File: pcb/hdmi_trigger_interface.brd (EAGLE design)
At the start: 78.7 x 63.5 mm, 58 parts, among them U1 TPD12S016PWR, U2 TPD12S016PWR, Y1 SI514

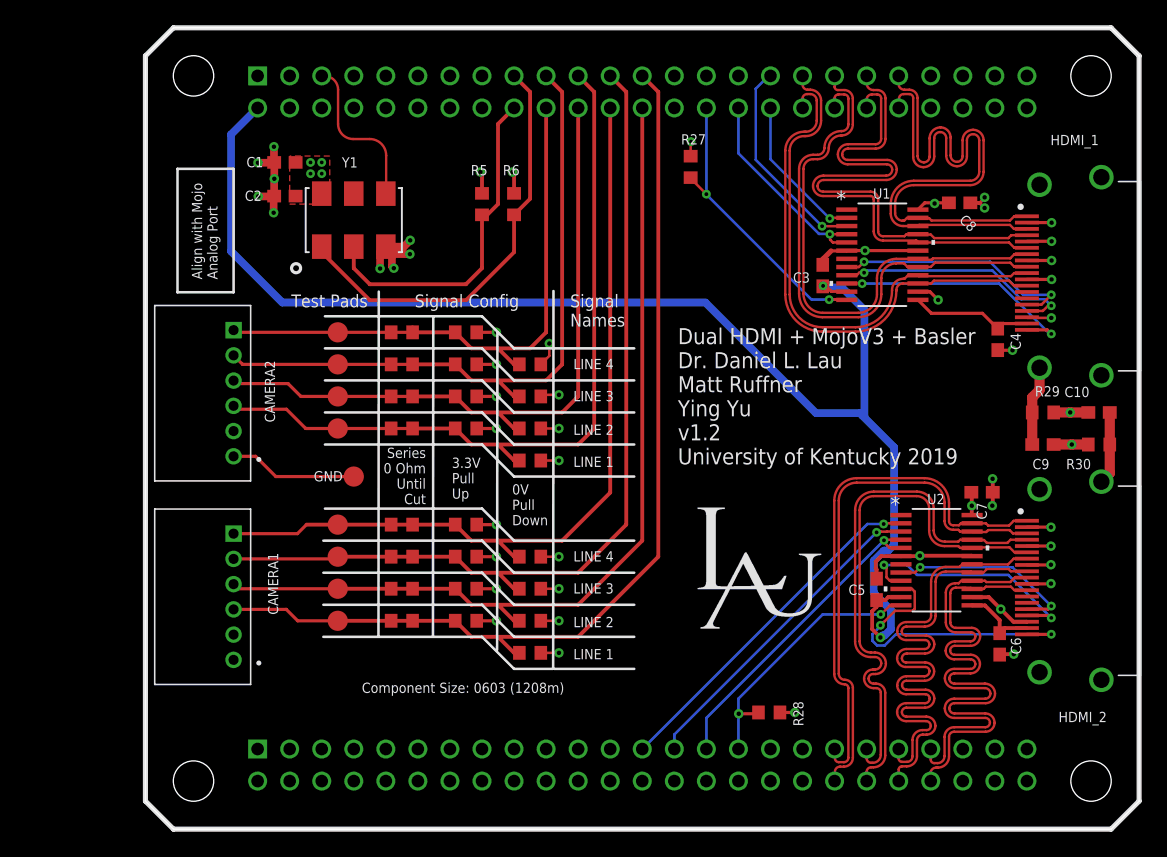
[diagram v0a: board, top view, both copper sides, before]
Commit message: ripped up old diff pairs, ready to route new 8/8 lines
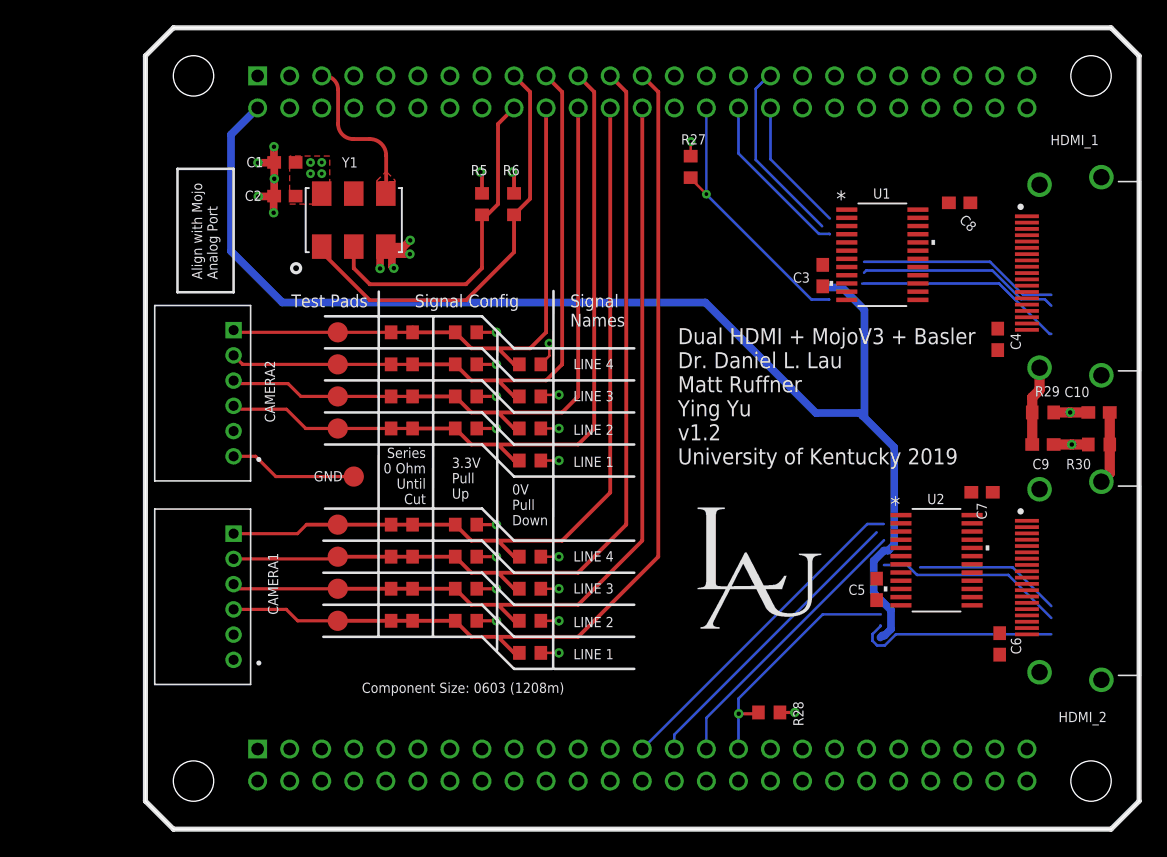
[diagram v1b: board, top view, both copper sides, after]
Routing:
- net GND: track 92.9 -> 43.9 mm, vias 38 -> 19
- net D22_N: track 41.6 -> 0.00 mm
- net D22_P: track 41.6 -> 0.00 mm
- net D11_P: track 41.4 -> 0.00 mm
- net D11_N: track 41.4 -> 0.00 mm
- net D12_P: track 41.2 -> 0.00 mm
- net D12_N: track 41.2 -> 0.00 mm
- net D01_N: track 41.2 -> 0.00 mm
- net D21_N: track 41.1 -> 0.00 mm
- net D01_P: track 41.1 -> 0.00 mm
- net D21_P: track 41.1 -> 0.00 mm
- net CLK1_P: track 41.0 -> 0.00 mm
- net CLK1_N: track 40.9 -> 0.00 mm
- net D02_N: track 40.8 -> 0.00 mm
- net CLK2_P: track 40.8 -> 0.00 mm
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- added copper zone on layer 1, net PROG_CLK

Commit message: one hdmi port routed, one to go. net class made with 8/8 mil trace width and spacing
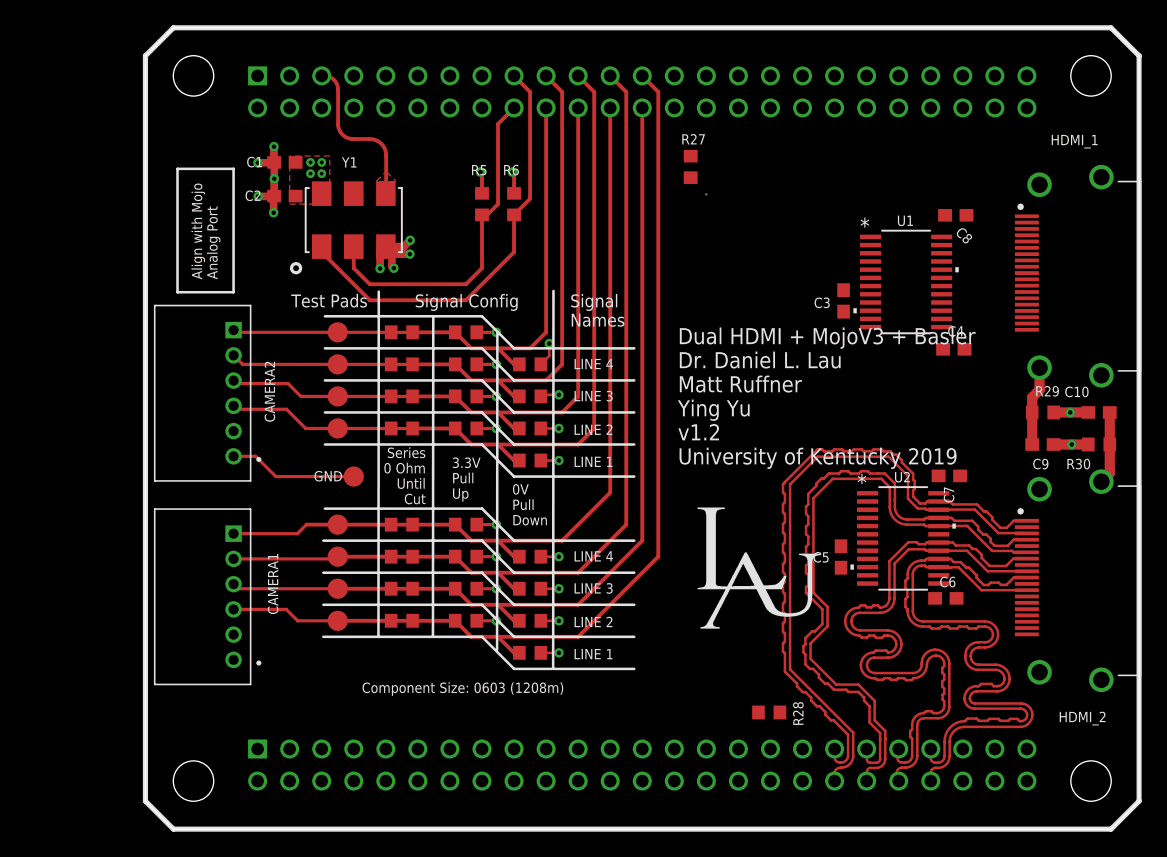
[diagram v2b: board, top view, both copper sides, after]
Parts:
- moved C6 5.59 mm to (63.4, 18.3), turned to 0 degrees
- moved C5 3.81 mm to (55.1, 21.6)
- moved C4 3.57 mm to (64.1, 38.0), turned to 0 degrees
- moved U2 3.16 mm to (60.0, 23.0)
- moved C7 2.90 mm to (63.7, 28.0)
- moved U1 2.86 mm to (60.3, 43.4)
- moved C3 2.60 mm to (55.3, 41.9)
- moved C8 1.04 mm to (64.2, 48.6)
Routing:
- net 5V: track 100.8 -> 0.00 mm
- net D22_P: track 0.00 -> 52.4 mm
- net D12_P: track 0.00 -> 51.4 mm
- net CLK2_P: track 0.00 -> 49.9 mm
- net D22_N: track 0.00 -> 49.5 mm
- net D02_P: track 0.00 -> 49.2 mm
- net D12_N: track 0.00 -> 48.9 mm
- net CLK2_N: track 0.00 -> 47.9 mm
- net D02_N: track 0.00 -> 46.7 mm
- net SCL2_M: track 26.5 -> 0.00 mm
- net SDA2_M: track 23.8 -> 0.00 mm
- net HP2_M: track 22.4 -> 0.00 mm
- net CTHPD1: track 21.9 -> 0.08 mm, vias 1 -> 0
- net CTHPD2: track 19.7 -> 0.14 mm, vias 1 -> 0
- net HP1: track 16.6 -> 0.00 mm
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
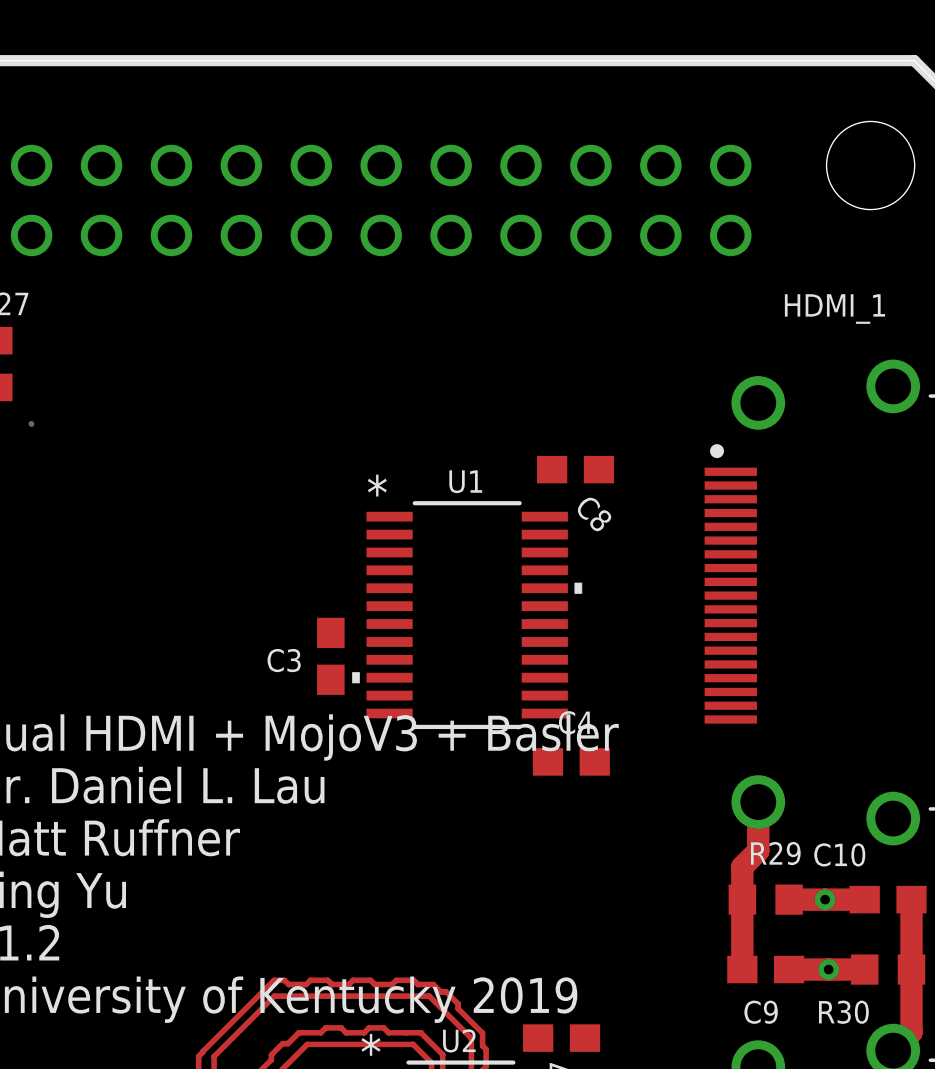
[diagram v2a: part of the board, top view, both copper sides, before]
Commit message: started routing second hdmi port
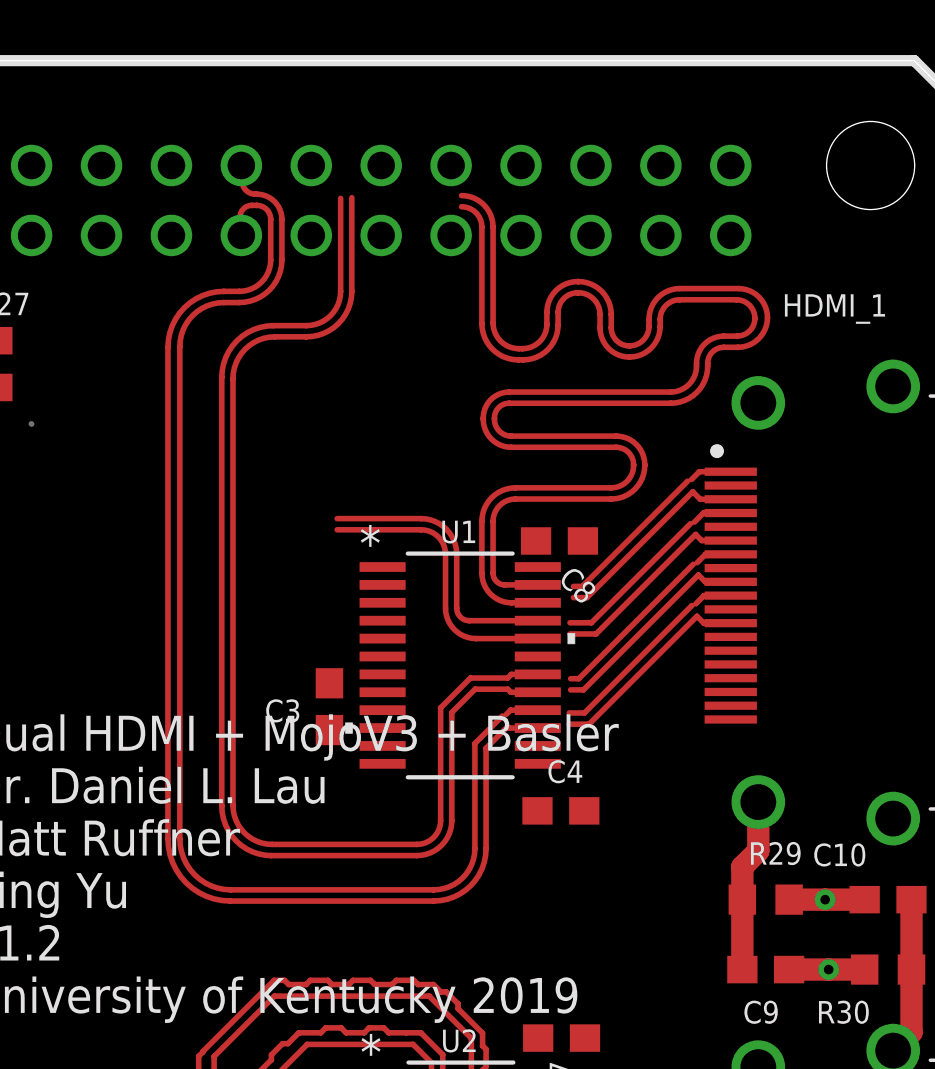
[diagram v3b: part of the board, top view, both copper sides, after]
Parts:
- moved C8 2.66 mm to (63.6, 46.1)
- moved U1 1.85 mm to (60.0, 41.5)
- moved C3 1.83 mm to (55.3, 40.0)
- moved C4 1.82 mm to (63.7, 36.2)
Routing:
- net D21_N: track 0.00 -> 54.6 mm
- net D21_P: track 0.00 -> 54.4 mm
- net CLK1_N: track 0.00 -> 53.3 mm
- net CLK1_P: track 0.00 -> 53.0 mm
- net D01_N: track 0.00 -> 49.3 mm
- net D01_P: track 0.00 -> 48.7 mm
- net D11_N: track 0.00 -> 17.5 mm
- net D11_P: track 0.00 -> 17.3 mm

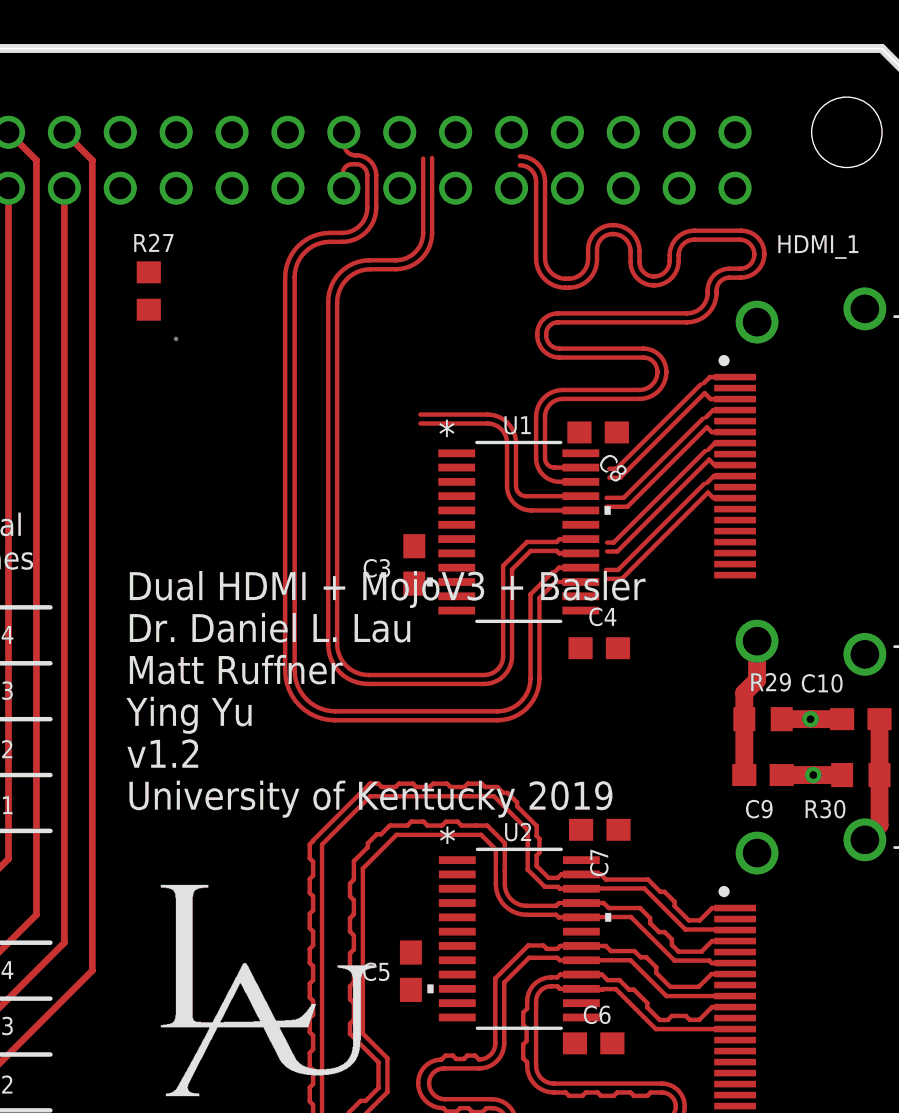
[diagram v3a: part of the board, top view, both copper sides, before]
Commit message: work on routing second hdmi port
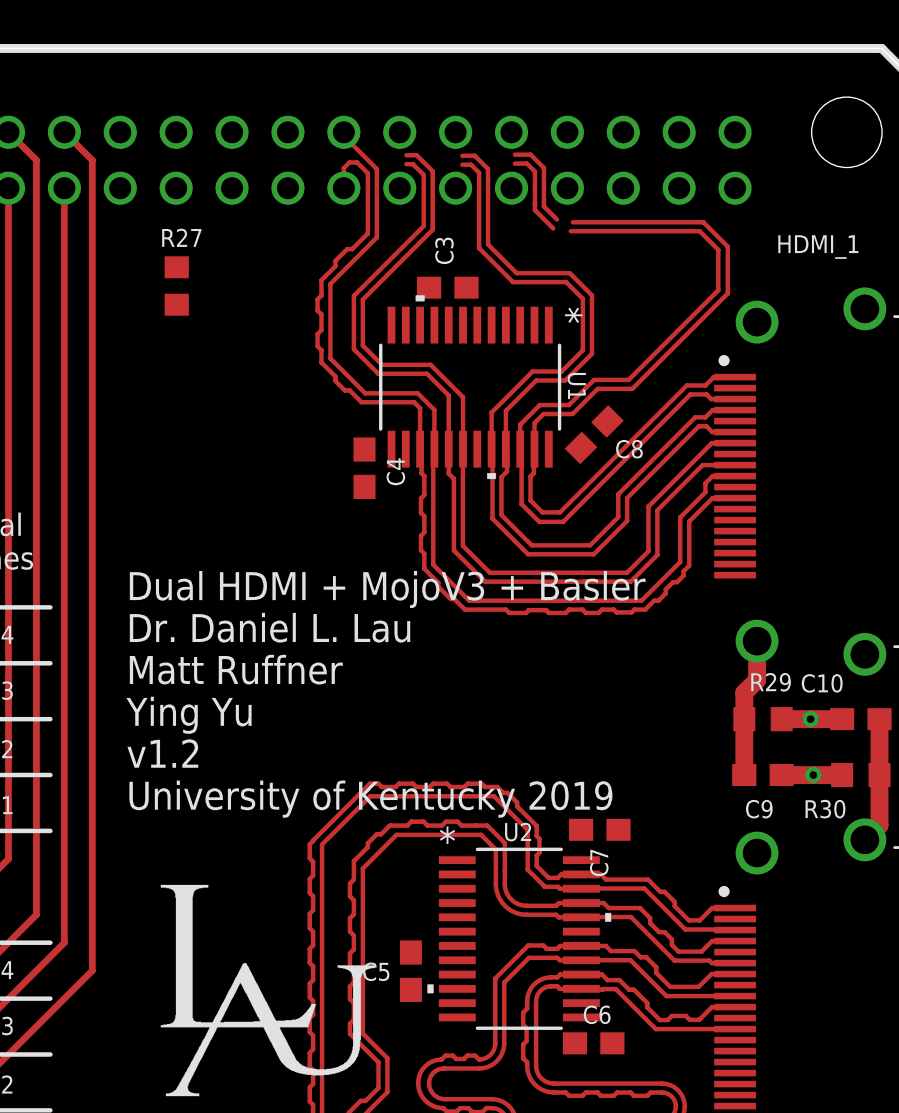
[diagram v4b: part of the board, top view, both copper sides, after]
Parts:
- moved C4 13.4 mm to (53.0, 44.4), turned to 270 degrees
- moved C3 12.7 mm to (56.8, 52.6), turned to 0 degrees
- moved U1 6.94 mm to (57.8, 48.1), turned to 270 degrees
- moved R27 1.29 mm to (44.5, 52.7)
- moved C8 0.20 mm to (63.4, 45.9), turned to 45 degrees
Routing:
- net D11_P: track 17.3 -> 37.4 mm
- net D11_N: track 17.5 -> 37.3 mm
- net D21_N: track 54.6 -> 40.7 mm
- net D21_P: track 54.4 -> 40.7 mm
- net CLK1_P: track 53.0 -> 42.7 mm
- net D01_N: track 49.3 -> 39.5 mm
- net D01_P: track 48.7 -> 39.5 mm
- net CLK1_N: track 53.3 -> 44.3 mm

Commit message: more work on length tuning
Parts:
- moved C3 14.1 mm to (43.4, 48.4)
- moved C4 12.1 mm to (42.9, 37.8)
- moved R27 11.1 mm to (45.2, 41.6)
- moved U1 8.14 mm to (50.6, 44.2), turned to 0 degrees
- moved C8 8.12 mm to (56.0, 49.1)
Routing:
- net D11_N: track 37.3 -> 41.5 mm
- net CLK1_P: track 42.7 -> 39.9 mm
- net D11_P: track 37.4 -> 39.6 mm
- net D21_P: track 40.7 -> 38.6 mm
- net N$13: track 6.33 -> 4.55 mm
- net CLK1_N: track 44.3 -> 42.7 mm
- net D01_N: track 39.5 -> 40.9 mm
- net D01_P: track 39.5 -> 38.8 mm
- net D21_N: track 40.7 -> 41.4 mm

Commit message: more routing
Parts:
- added X1, X2: 87438-06, con-molex:87438-06
- moved R27 12.5 mm to (43.6, 54.0), turned to 0 degrees
- moved C4 12.2 mm to (54.9, 39.7), turned to 0 degrees
- moved C3 5.84 mm to (45.3, 42.9), turned to 90 degrees
- moved CAMERA2 4.05 mm to (2.95, 34.3)
- moved C5 0.57 mm to (54.6, 21.9)
- moved C8 0.49 mm to (56.3, 49.4)
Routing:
- net GND: track 43.9 -> 79.1 mm, vias 19 -> 31
- net SCL2_M: track 0.00 -> 29.2 mm, vias 0 -> 1
- net SDA2_M: track 0.00 -> 27.1 mm, vias 0 -> 1
- net HP2_M: track 0.00 -> 26.7 mm, vias 0 -> 1
- net SCL1: track 0.00 -> 25.4 mm
- net SDA1: track 0.00 -> 25.3 mm
- net HP1: track 0.00 -> 24.7 mm
- net CTHPD1: track 0.06 -> 20.2 mm
- net CTHPD2: track 0.14 -> 19.7 mm, vias 0 -> 2
- net HP2: track 0.00 -> 18.6 mm, vias 0 -> 2
- net SCL2: track 0.00 -> 17.9 mm, vias 0 -> 2
- net SDA2: track 0.00 -> 17.7 mm, vias 0 -> 2
- net 5VHDMI1: track 0.00 -> 17.5 mm, vias 0 -> 2
- net HP1_M: track 0.00 -> 17.0 mm
- net SDA1_M: track 0.00 -> 17.0 mm
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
